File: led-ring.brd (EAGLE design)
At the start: 116.5 x 103 mm, 33 parts, among them IC8 MCP23017, X1 78127-1128, X2 78127-1128

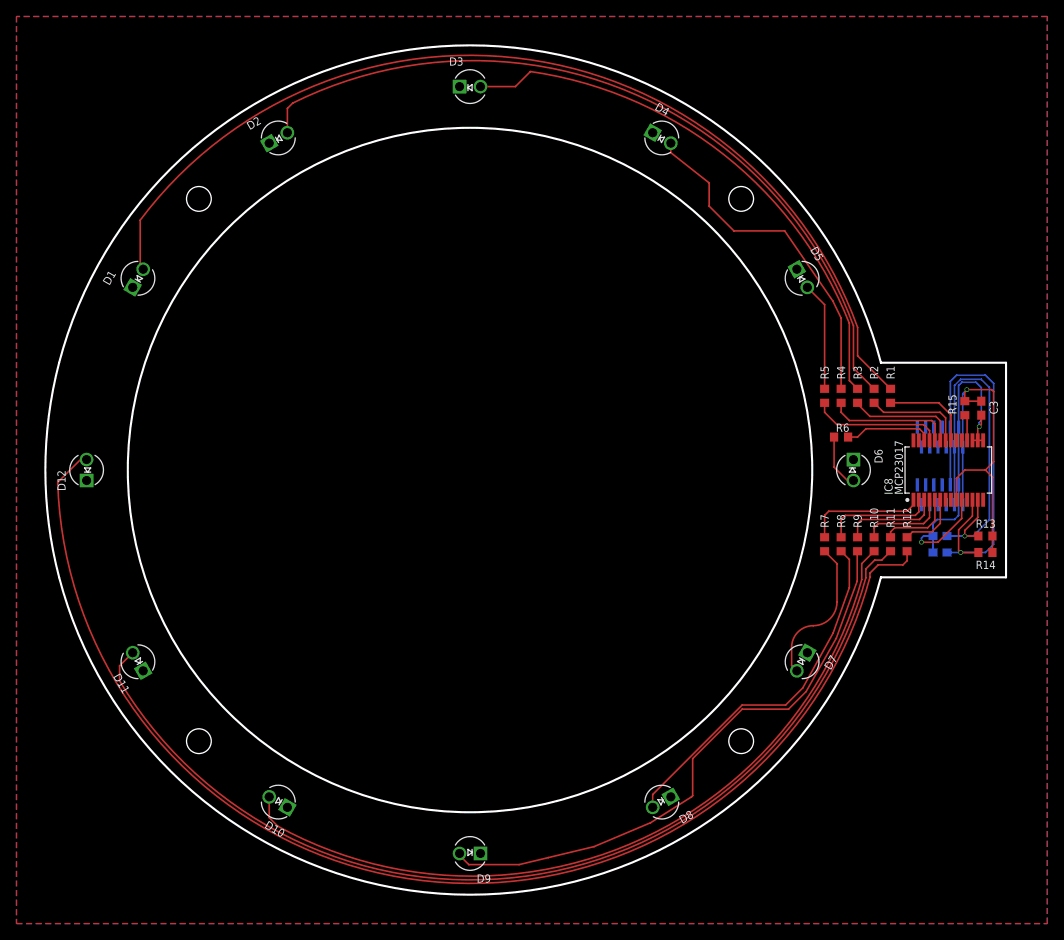
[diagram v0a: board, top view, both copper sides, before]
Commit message: changed some footprint drawings
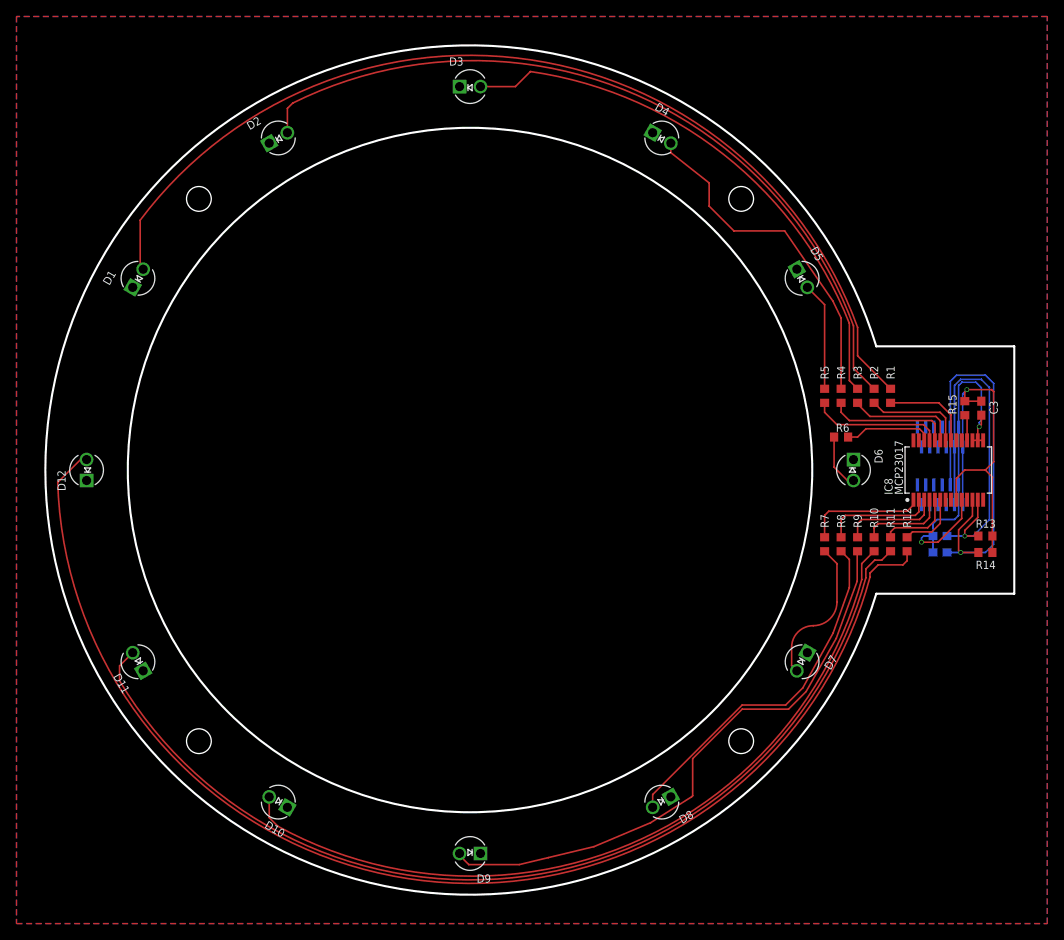
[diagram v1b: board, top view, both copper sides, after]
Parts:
- added U$1: (no value), frames:A4L-LOC
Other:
- board size 116.5 x 103 mm -> 117.5 x 103 mm
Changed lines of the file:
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@@
 <drawing>
 <settings>
-<setting alwaysvectorfont="no"/>
+<setting alwaysvectorfont="yes"/>
 <setting verticaltext="up"/>
 </settings>
-<grid distance="5" unitdist="mm" unit="mm" style="lines" multiple="1" display="yes" altdistance="0.25" altunitdist="mm" altunit="mm"/>
+<grid distance="1" unitdist="mm" unit="mm" style="lines" multiple="1" display="yes" altdistance="0.25" altunitdist="mm" altunit="mm"/>
 <layers>
 <layer number="1" name="Top" color="4" fill="1" visible="yes" active="yes"/>
@@
 <layer number="25" name="tNames" color="7" fill="1" visible="yes" active="yes"/>
 <layer number="26" name="bNames" color="7" fill="1" visible="yes" active="yes"/>
-<layer number="27" name="tValues" color="7" fill="1" visible="yes" active="yes"/>
-<layer number="28" name="bValues" color="7" fill="1" visible="yes" active="yes"/>
+<layer number="27" name="tValues" color="7" fill="1" visible="no" active="yes"/>
+<layer number="28" name="bValues" color="7" fill="1" visible="no" active="yes"/>
 <layer number="29" name="tStop" color="7" fill="3" visible="no" active="yes"/>
 <layer number="30" name="bStop" color="7" fill="6" visible="no" active="yes"/>
@@
 <layer number="41" name="tRestrict" color="4" fill="10" visible="yes" active="yes"/>
 <layer number="42" name="bRestrict" color="1" fill="10" visible="yes" active="yes"/>
-<layer number="43" name="vRestrict" color="2" fill="10" visible="yes" active="yes"/>
+<layer number="43" name="vRestrict" color="2" fill="10" visible="no" active="yes"/>
 <layer number="44" name="Drills" color="7" fill="1" visible="no" active="yes"/>
 <layer number="45" name="Holes" color="7" fill="1" visible="no" active="yes"/>
@@
 <layer number="47" name="Measures" color="7" fill="1" visible="no" active="yes"/>
 <layer number="48" name="Document" color="7" fill="1" visible="yes" active="yes"/>
-<layer number="49" name="Reference" color="7" fill="1" visible="yes" active="yes"/>
+<layer number="49" name="Reference" color="7" fill="1" visible="no" active="yes"/>
 <layer number="50" name="dxf" color="7" fill="1" visible="no" active="no"/>
 <layer number="51" name="tDocu" color="7" fill="1" visible="yes" active="yes"/>
@@
 </layers>
 <board>
+<fusionsync huburn="a.YnVzaW5lc3M6ZGJkcGxhc21h" projecturn="a.YnVzaW5lc3M6ZGJkcGxhc21hIzIwMTgwMjA2MTE2NDkxODU2" f3durn="urn:adsk.wipprod:dm.lineage:0d6icMchTCarPJLupLpU6g" pcbguid="44db56b8-18dc-41bd-80a2-d615f9febae1" lastpulledtime="2019-07-03T21:08:23Z" lastsyncedchangeguid="292105d6-c618-90e7-f5e6-e1d0755c615a"/>
 <plain>
-<text x="42" y="-12" size="1" layer="26" font="vector" rot="MR0" align="bottom-right">30.06.2019
+<text x="42" y="-13" size="1" layer="26" font="vector" rot="MR0" align="bottom-right">30.06.2019
 v0.1.0
 https://github.com/
 hansachterbahn/led-ring</text>
-<text x="43" y="5" size="1.3" layer="26" font="vector" ratio="12" rot="MR0" align="bottom-right">LED Ring
+<text x="42" y="9" size="1.3" layer="26" font="vector" ratio="12" rot="MR0" align="bottom-right">LED Ring
 by h8</text>
+<dimension x1="-0.000240625" y1="0" x2="-48.85680625" y2="16.285784375" x3="-24.428521875" y3="8.14289375" textsize="1.778" layer="48" dtype="radius"/>
+<dimension x1="0" y1="0" x2="-41.5" y2="0" x3="-20.75" y3="0" textsize="1.778" layer="48" dtype="radius"/>
 <hole x="-32.88" y="32.88" drill="3"/>
 <hole x="32.88" y="-32.88" drill="3"/>
 <hole x="32.88" y="32.88" drill="3"/>
 <hole x="-32.88" y="-32.88" drill="3"/>
-<wire x1="49.829" y1="13.011" x2="-49.829" y2="13.011" width="0.254" layer="20" curve="150.732"/>
-<wire x1="65" y1="13.011" x2="49.829" y2="13.011" width="0.254" layer="20"/>
-<wire x1="65" y1="-13.011" x2="65" y2="13.011" width="0.254" layer="20"/>
-<wire x1="49.829" y1="-13.011" x2="65" y2="-13.011" width="0.254" layer="20"/>
-<wire x1="-49.829" y1="-13.011" x2="49.829" y2="-13.011" width="0.254" layer="20" curve="150.732"/>
-<wire x1="-49.829" y1="13.011" x2="-49.829" y2="-13.011" width="0.254" layer="20" curve="29.268"/>
+<wire x1="66" y1="15" x2="49.267" y2="15" width="0.254" layer="20"/>
+<wire x1="49.267" y1="15" x2="49.267" y2="-15" width="0.254" layer="20" curve="326.133"/>
+<wire x1="49.267" y1="-15" x2="66" y2="-15" width="0.254" layer="20"/>
+<wire x1="66" y1="-15" x2="66" y2="15" width="0.254" layer="20"/>
 <circle x="0" y="0" radius="41.5" width="0.254" layer="20"/>
 </plain>
@@
 <attribute name="VALUE" x="57.635" y="-9.905" size="1.27" layer="28" rot="MR0"/>
 </element>
+<element name="U$1" library="frames" library_urn="urn:adsk.eagle:library:229" package="A4L-LOC" value="" x="-120" y="-94" smashed="yes">
+<attribute name="DRAWING_NAME" x="97.17" y="-78.76" size="2.54" layer="48" font="vector"/>
+<attribute name="LAST_DATE_TIME" x="97.17" y="-83.84" size="2.286" layer="48" font="vector"/>
+</element>
 </elements>
 <signals>
@@
 </note>
 <note version="8.3" severity="warning">
+Since Version 8.3, EAGLE supports Fusion synchronisation.
+This feature will not be available in this version and saving
+the document will break the link to the Fusion PCB feature.
+</note>
+<note version="8.3" severity="warning">
